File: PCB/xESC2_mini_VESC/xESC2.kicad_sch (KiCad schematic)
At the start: 52 parts, among them J1 Conn_01x06_Male, J2 U254-051T-4BH83-F1S, J3 Conn_01x05_Male, J4 Conn_01x05_Male, J5 Conn_01x03_Male, U5 SN65HVD232

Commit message: BoM data updates
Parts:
- C15, C27, C28, C29, C30, C31, C45, C46, C47, FID1, FID2, FID3, FID4, FID5, FID6, FID7, FID8: Config (none) -> do not place
- J1: LCSC (none) -> C2935912; Part Number (none) -> DZ254R-11-06-63; Stock_PN (none) -> J-TH-1x6-.1
- J3, J4: LCSC (none) -> C2935911; Part Number (none) -> DZ254R-11-05-63; Stock_PN (none) -> J-TH-1x5-.1
- J5: LCSC (none) -> C2935909; Part Number (none) -> DZ254R-11-05-63; Stock_PN (none) -> J-TH-1x3-.1
- R17, R19, R21, R24, R26, R28, R40: Digikey RC0603FR-071K5L -> 311-1.50KHRCT-ND; Part Number 311-1.50KHRCT-ND -> RC0603FR-071K5L
- R18, R20, R22, R33, R34, R35: Digikey RC0603FR-072K2L -> 311-2.20KHRCT-ND; Part Number 311-2.20KHRCT-ND -> RC0603FR-072K2L
- R23, R25, R27, R39: Digikey RMCF0603FT22K0 -> RMCF0603FT22K0CT-ND; Part Number RMCF0603FT22K0CT-ND -> RMCF0603FT22K0
- R30, R41: Digikey RC0603FR-0710KL -> 311-10.0KHRCT-ND; Part Number 311-10.0KHRCT-ND -> RC0603FR-0710KL
- R31, R32: Digikey RMCF0603FT22R0 -> RMCF0603FT22R0CT-ND; Part Number RMCF0603FT22R0CT-ND -> RMCF0603FT22R0
- R36: Digikey RMCF0603FT120R -> RMCF0603FT120RCT-ND; Part Number RMCF0603FT120RCT-ND -> RMCF0603FT120R
- R37, R38: Digikey RC0603FR-07150RL -> 311-150HRCT-ND; Part Number 311-150HRCT-ND -> RC0603FR-07150RL

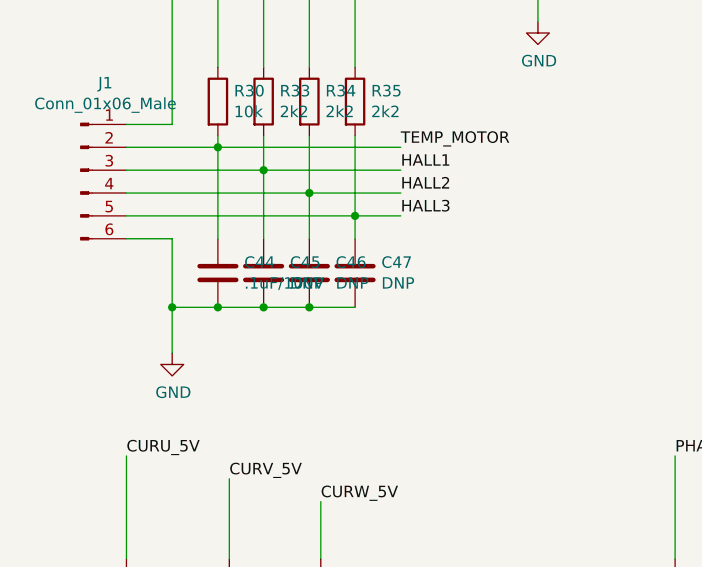
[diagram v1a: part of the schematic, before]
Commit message: updated BOM for .1uF caps
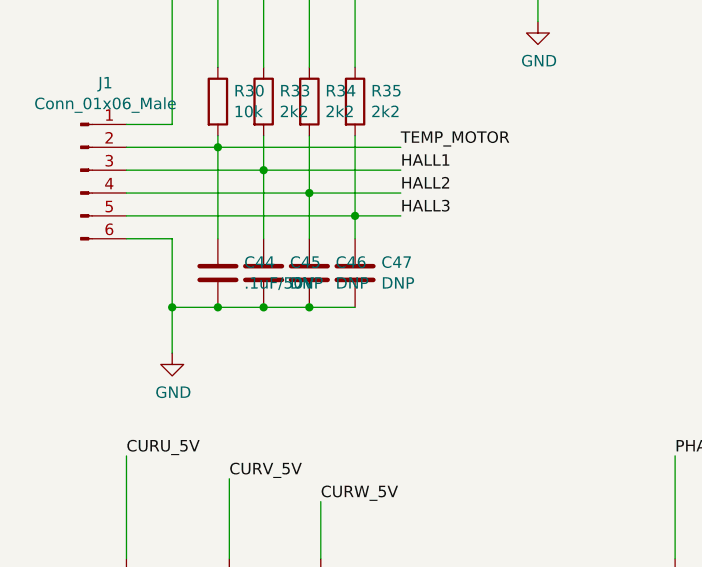
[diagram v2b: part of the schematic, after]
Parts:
- C44: value .1uF/100V -> .1uF/50V; Digikey 490-1331-1-ND -> 1276-1935-1-ND
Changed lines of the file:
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@@
       (effects (font (size 1.27 1.27)) (justify left))
     )
-    (property "Value" ".1uF/100V" (id 1) (at 39.751 128.143 0)
+    (property "Value" ".1uF/50V" (id 1) (at 39.751 128.143 0)
       (effects (font (size 1.27 1.27)) (justify left))
     )
@@
       (effects (font (size 1.27 1.27)) hide)
     )
-    (property "Digikey" "490-1331-1-ND" (id 4) (at 36.83 127 0)
+    (property "Digikey" "1276-1935-1-ND" (id 4) (at 36.83 127 0)
       (effects (font (size 1.27 1.27)) hide)
     )
@@
     )
     (path "/00000000-0000-0000-0000-000061a3f4e8/00000000-0000-0000-0000-000061a7e7a1"
-      (reference "C6") (unit 1) (value ".1uF/100V") (footprint "Capacitor_SMD:C_0603_1608Metric")
+      (reference "C6") (unit 1) (value ".1uF/50V") (footprint "Capacitor_SMD:C_0603_1608Metric")
     )
     (path "/00000000-0000-0000-0000-000061a3f4e8/00000000-0000-0000-0000-000061a6a715"
-      (reference "C7") (unit 1) (value ".1uF/100V") (footprint "Capacitor_SMD:C_0603_1608Metric")
+      (reference "C7") (unit 1) (value ".1uF/50V") (footprint "Capacitor_SMD:C_0603_1608Metric")
     )
     (path "/00000000-0000-0000-0000-000061a3f4e8/00000000-0000-0000-0000-000061a4478e"
@@
     )
     (path "/00000000-0000-0000-0000-000061ac26fb/00000000-0000-0000-0000-000061a8999f"
-      (reference "C34") (unit 1) (value ".1uF/100V") (footprint "Capacitor_SMD:C_0603_1608Metric")
+      (reference "C34") (unit 1) (value ".1uF/50V") (footprint "Capacitor_SMD:C_0603_1608Metric")
     )
     (path "/00000000-0000-0000-0000-000061ac26fb/00000000-0000-0000-0000-000061a7737f"
@@
     )
     (path "/00000000-0000-0000-0000-000061ac26fb/00000000-0000-0000-0000-000061a7d515"
-      (reference "C37") (unit 1) (value ".1uF/100V") (footprint "Capacitor_SMD:C_0603_1608Metric")
+      (reference "C37") (unit 1) (value ".1uF/50V") (footprint "Capacitor_SMD:C_0603_1608Metric")
     )
     (path "/00000000-0000-0000-0000-000061ac26fb/00000000-0000-0000-0000-000061a7c449"
@@
     )
     (path "/00000000-0000-0000-0000-000061ac26fb/00000000-0000-0000-0000-000061a6df2f"
-      (reference "C40") (unit 1) (value ".1uF/100V") (footprint "Capacitor_SMD:C_0603_1608Metric")
+      (reference "C40") (unit 1) (value ".1uF/50V") (footprint "Capacitor_SMD:C_0603_1608Metric")
     )
     (path "/00000000-0000-0000-0000-000061ac26fb/00000000-0000-0000-0000-000061a6e1b7"
-      (reference "C41") (unit 1) (value ".1uF/100V") (footprint "Capacitor_SMD:C_0603_1608Metric")
+      (reference "C41") (unit 1) (value ".1uF/50V") (footprint "Capacitor_SMD:C_0603_1608Metric")
     )
     (path "/00000000-0000-0000-0000-000061ac26fb/00000000-0000-0000-0000-000061a6e65e"
-      (reference "C42") (unit 1) (value ".1uF/100V") (footprint "Capacitor_SMD:C_0603_1608Metric")
+      (reference "C42") (unit 1) (value ".1uF/50V") (footprint "Capacitor_SMD:C_0603_1608Metric")
     )
     (path "/00000000-0000-0000-0000-000061ac26fb/00000000-0000-0000-0000-000061a6e9cb"
-      (reference "C43") (unit 1) (value ".1uF/100V") (footprint "Capacitor_SMD:C_0603_1608Metric")
+      (reference "C43") (unit 1) (value ".1uF/50V") (footprint "Capacitor_SMD:C_0603_1608Metric")
     )
     (path "/00000000-0000-0000-0000-000061ac0036"
-      (reference "C44") (unit 1) (value ".1uF/100V") (footprint "Capacitor_SMD:C_0603_1608Metric")
+      (reference "C44") (unit 1) (value ".1uF/50V") (footprint "Capacitor_SMD:C_0603_1608Metric")
     )
     (path "/00000000-0000-0000-0000-000061b68b12"
